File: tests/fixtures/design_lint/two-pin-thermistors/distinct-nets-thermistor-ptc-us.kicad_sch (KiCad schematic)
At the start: 1 part

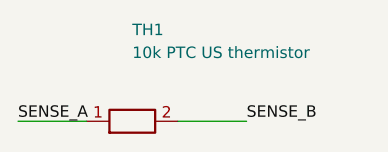
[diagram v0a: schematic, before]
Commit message: fix(lint): normalize thermistor fixture values
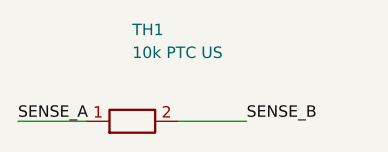
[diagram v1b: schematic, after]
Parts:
- TH1: value 10k PTC US thermistor -> 10k PTC US
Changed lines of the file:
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@@
     (in_bom yes) (on_board yes) (dnp no)
     (property "Reference" "TH1" (at 63.50 53.34 0) (effects (font (size 1.27 1.27)) (justify left)))
-    (property "Value" "10k PTC US thermistor" (at 63.50 55.88 0) (effects (font (size 1.27 1.27)) (justify left)))
+    (property "Value" "10k PTC US" (at 63.50 55.88 0) (effects (font (size 1.27 1.27)) (justify left)))
     (property "Footprint" "Synthetic:Thermistor" (at 63.50 63.50 0) (effects (font (size 1.27 1.27)) hide))
     (property "Datasheet" "" (at 63.50 63.50 0) (effects (font (size 1.27 1.27)) hide))
